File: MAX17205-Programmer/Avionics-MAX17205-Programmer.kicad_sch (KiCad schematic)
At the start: 2 parts, among them J1 Conn_01x05, J2 95009-7661

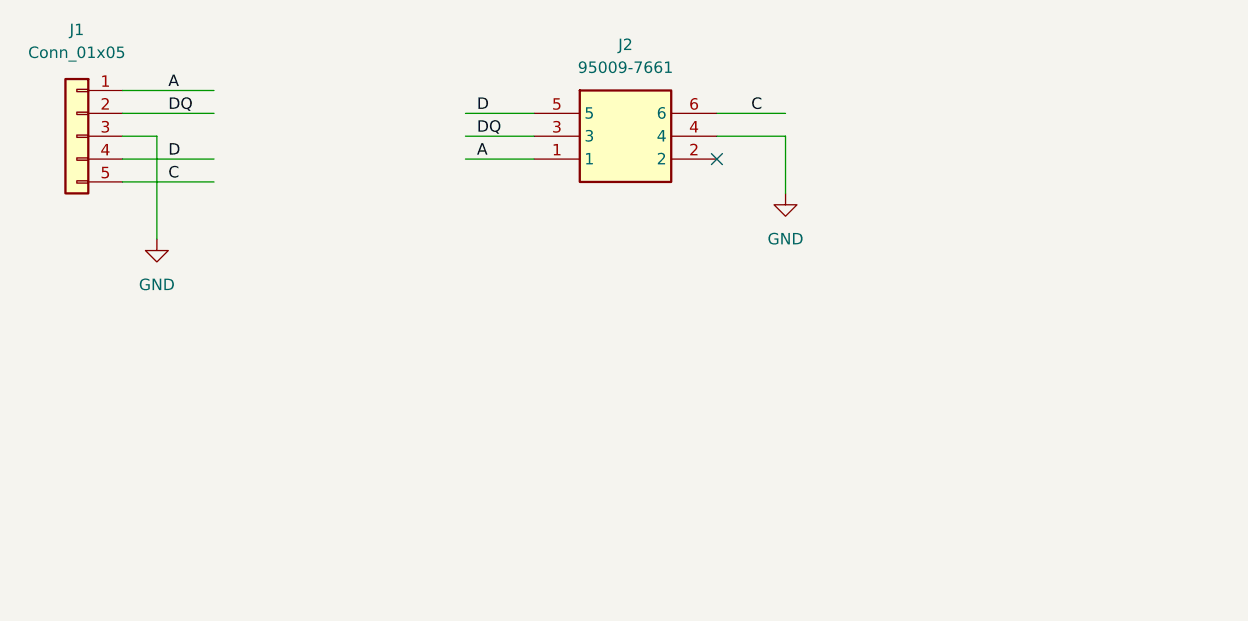
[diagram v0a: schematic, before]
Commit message: Updated FPC connector
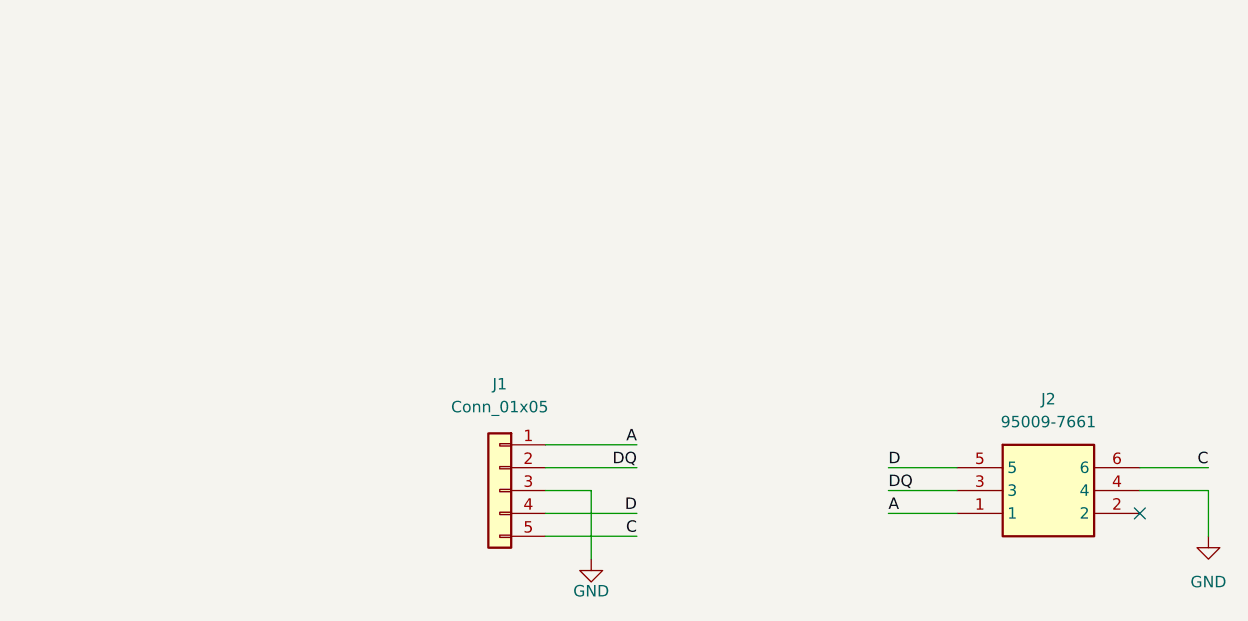
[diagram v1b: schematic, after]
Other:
- moved on the sheet: J1, J2
